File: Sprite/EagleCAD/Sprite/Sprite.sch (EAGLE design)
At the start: 32 parts, among them P1 SPRITE_PIN, P2 SPRITE_PIN, U1 CC430F5137, U2 HMC5883LSMD, U3 ITG-3200

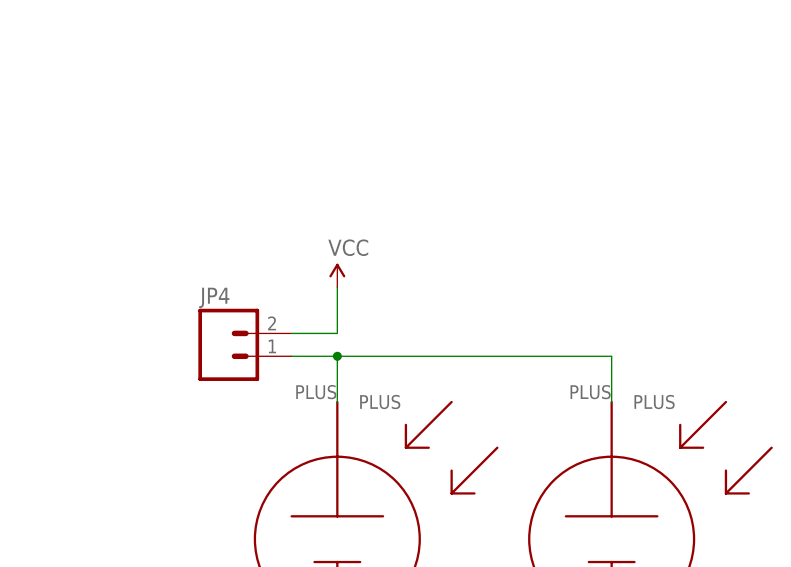
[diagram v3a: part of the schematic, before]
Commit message: Made corner hole 2.8 mm
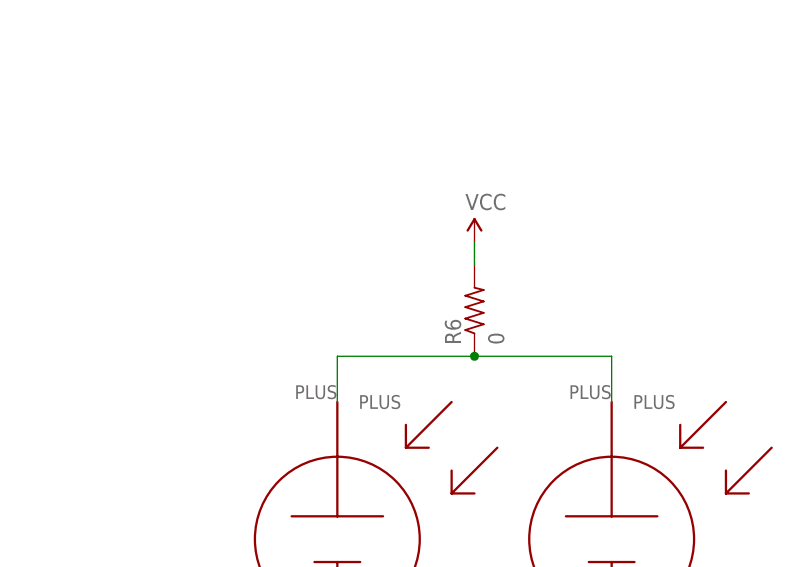
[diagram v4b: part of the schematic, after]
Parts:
- removed JP4: (no value), SparkFun:M02PTH
- added R6: 0, rcl:R-US_R0805
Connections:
- net VCC: now also R6.2; no longer JP4.2
- net VSOLAR: now also R6.1; no longer JP4.1
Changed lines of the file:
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@@
 <part name="GND10" library="SparkFun" deviceset="GND" device=""/>
 <part name="R5" library="SparkFun" deviceset="RESISTOR" device="0603-RES" value="270R"/>
-<part name="JP4" library="SparkFun" deviceset="M02" device="PTH"/>
 <part name="JP3" library="SparkFun" deviceset="M02" device="PTH"/>
-<part name="S2" library="TASC" deviceset="TASC" device=""/>
 <part name="U$1" library="SpriteTCXO" deviceset="TCXO_7Z" device=""/>
 <part name="P+11" library="SparkFun" deviceset="VCC" device=""/>
@@
 <part name="P1" library="SpritePin" deviceset="SPRITE_PIN" device=""/>
 <part name="S1" library="TASC" deviceset="TASC" device=""/>
+<part name="S2" library="TASC" deviceset="TASC" device=""/>
+<part name="R6" library="rcl" deviceset="R-US_" device="R0805" value="0"/>
 </parts>
 <sheets>
@@
 <instances>
 <instance part="GND1" gate="1" x="347.98" y="66.04"/>
-<instance part="P+1" gate="1" x="332.74" y="114.3"/>
+<instance part="P+1" gate="1" x="347.98" y="119.38"/>
 <instance part="U1" gate="G$1" x="152.4" y="86.36"/>
 <instance part="C1" gate="G$1" x="228.6" y="55.88" rot="R90"/>
@@
 <instance part="GND10" gate="1" x="86.36" y="99.06"/>
 <instance part="R5" gate="G$1" x="104.14" y="104.14"/>
-<instance part="JP4" gate="G$1" x="320.04" y="106.68"/>
 <instance part="JP3" gate="G$1" x="114.3" y="88.9" rot="MR180"/>
-<instance part="S2" gate="G$1" x="332.74" y="86.36"/>
 <instance part="U$1" gate="G$1" x="241.3" y="50.8" rot="MR0"/>
 <instance part="P+11" gate="1" x="251.46" y="48.26"/>
 <instance part="P2" gate="G$1" x="127" y="144.78"/>
 <instance part="P1" gate="G$1" x="127" y="137.16"/>
-<instance part="S1" gate="G$1" x="363.22" y="86.36"/>
+<instance part="S1" gate="G$1" x="332.74" y="86.36"/>
+<instance part="S2" gate="G$1" x="363.22" y="86.36"/>
+<instance part="R6" gate="G$1" x="347.98" y="111.76" rot="R90"/>
 </instances>
 <busses>
@@
 </segment>
 <segment>
-<pinref part="JP4" gate="G$1" pin="2"/>
 <pinref part="P+1" gate="1" pin="VCC"/>
-<wire x1="327.66" y1="109.22" x2="332.74" y2="109.22" width="0.1524" layer="91"/>
-<wire x1="332.74" y1="109.22" x2="332.74" y2="114.3" width="0.1524" layer="91"/>
+<pinref part="R6" gate="G$1" pin="2"/>
+<wire x1="347.98" y1="116.84" x2="347.98" y2="119.38" width="0.1524" layer="91"/>
 </segment>
 <segment>
@@
 </segment>
 <segment>
-<pinref part="S2" gate="G$1" pin="MINUS1"/>
 <wire x1="327.66" y1="71.12" x2="327.66" y2="68.58" width="0.1524" layer="91"/>
-<pinref part="S2" gate="G$1" pin="MINUS2"/>
 <wire x1="327.66" y1="68.58" x2="347.98" y2="68.58" width="0.1524" layer="91"/>
 <wire x1="347.98" y1="68.58" x2="337.82" y2="68.58" width="0.1524" layer="91"/>
@@
 <junction x="347.98" y="68.58"/>
 <junction x="337.82" y="68.58"/>
-<pinref part="S1" gate="G$1" pin="MINUS2"/>
 <wire x1="368.3" y1="71.12" x2="368.3" y2="68.58" width="0.1524" layer="91"/>
-<pinref part="S1" gate="G$1" pin="MINUS1"/>
 <wire x1="358.14" y1="71.12" x2="358.14" y2="68.58" width="0.1524" layer="91"/>
 <wire x1="368.3" y1="68.58" x2="358.14" y2="68.58" width="0.1524" layer="91"/>
@@
 <junction x="358.14" y="68.58"/>
 <junction x="368.3" y="68.58"/>
+<pinref part="S1" gate="G$1" pin="MINUS1"/>
+<pinref part="S1" gate="G$1" pin="MINUS2"/>
+<pinref part="S2" gate="G$1" pin="MINUS1"/>
+<pinref part="S2" gate="G$1" pin="MINUS2"/>
 </segment>
 <segment>
@@
 <net name="VSOLAR" class="0">
 <segment>
-<pinref part="JP4" gate="G$1" pin="1"/>
-<wire x1="327.66" y1="106.68" x2="332.74" y2="106.68" width="0.1524" layer="91"/>
+<wire x1="332.74" y1="101.6" x2="332.74" y2="106.68" width="0.1524" layer="91"/>
+<wire x1="363.22" y1="101.6" x2="363.22" y2="106.68" width="0.1524" layer="91"/>
+<wire x1="363.22" y1="106.68" x2="347.98" y2="106.68" width="0.1524" layer="91"/>
+<pinref part="S1" gate="G$1" pin="PLUS"/>
 <pinref part="S2" gate="G$1" pin="PLUS"/>
-<wire x1="332.74" y1="101.6" x2="332.74" y2="106.68" width="0.1524" layer="91"/>
-<pinref part="S1" gate="G$1" pin="PLUS"/>
-<wire x1="363.22" y1="101.6" x2="363.22" y2="106.68" width="0.1524" layer="91"/>
-<wire x1="363.22" y1="106.68" x2="332.74" y2="106.68" width="0.1524" layer="91"/>
-<junction x="332.74" y="106.68"/>
-</segment>
-</net>
+<pinref part="R6" gate="G$1" pin="1"/>
+<wire x1="347.98" y1="106.68" x2="332.74" y2="106.68" width="0.1524" layer="91"/>
+<junction x="347.98" y="106.68"/>
+</segment>
+</net>

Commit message: Updated Gerbers and BOM for new Sprite order
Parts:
- renumbered U$1 to X1
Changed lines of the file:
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@@
 <part name="R5" library="SparkFun" deviceset="RESISTOR" device="0603-RES" value="270R"/>
 <part name="JP3" library="SparkFun" deviceset="M02" device="PTH"/>
-<part name="U$1" library="SpriteTCXO" deviceset="TCXO_7Z" device=""/>
+<part name="X1" library="SpriteTCXO" deviceset="TCXO_7Z" device=""/>
 <part name="P+11" library="SparkFun" deviceset="VCC" device=""/>
 <part name="P2" library="SpritePin" deviceset="SPRITE_PIN" device=""/>
@@
 <instance part="R5" gate="G$1" x="104.14" y="104.14"/>
 <instance part="JP3" gate="G$1" x="114.3" y="88.9" rot="MR180"/>
-<instance part="U$1" gate="G$1" x="241.3" y="50.8" rot="MR0"/>
+<instance part="X1" gate="G$1" x="241.3" y="50.8" rot="MR0"/>
 <instance part="P+11" gate="1" x="251.46" y="48.26"/>
 <instance part="P2" gate="G$1" x="127" y="144.78"/>
@@
 </segment>
 <segment>
-<pinref part="U$1" gate="G$1" pin="VCC"/>
+<pinref part="X1" gate="G$1" pin="VCC"/>
 <pinref part="P+11" gate="1" pin="VCC"/>
 <wire x1="248.92" y1="45.72" x2="251.46" y2="45.72" width="0.1524" layer="91"/>
@@
 </segment>
 <segment>
-<pinref part="U$1" gate="G$1" pin="GND"/>
+<pinref part="X1" gate="G$1" pin="GND"/>
 <pinref part="GND8" gate="1" pin="GND"/>
 <wire x1="226.06" y1="45.72" x2="233.68" y2="45.72" width="0.1524" layer="91"/>
@@
 <segment>
 <pinref part="C1" gate="G$1" pin="2"/>
-<pinref part="U$1" gate="G$1" pin="OUT"/>
+<pinref part="X1" gate="G$1" pin="OUT"/>
 <wire x1="231.14" y1="55.88" x2="233.68" y2="55.88" width="0.1524" layer="91"/>
 </segment>

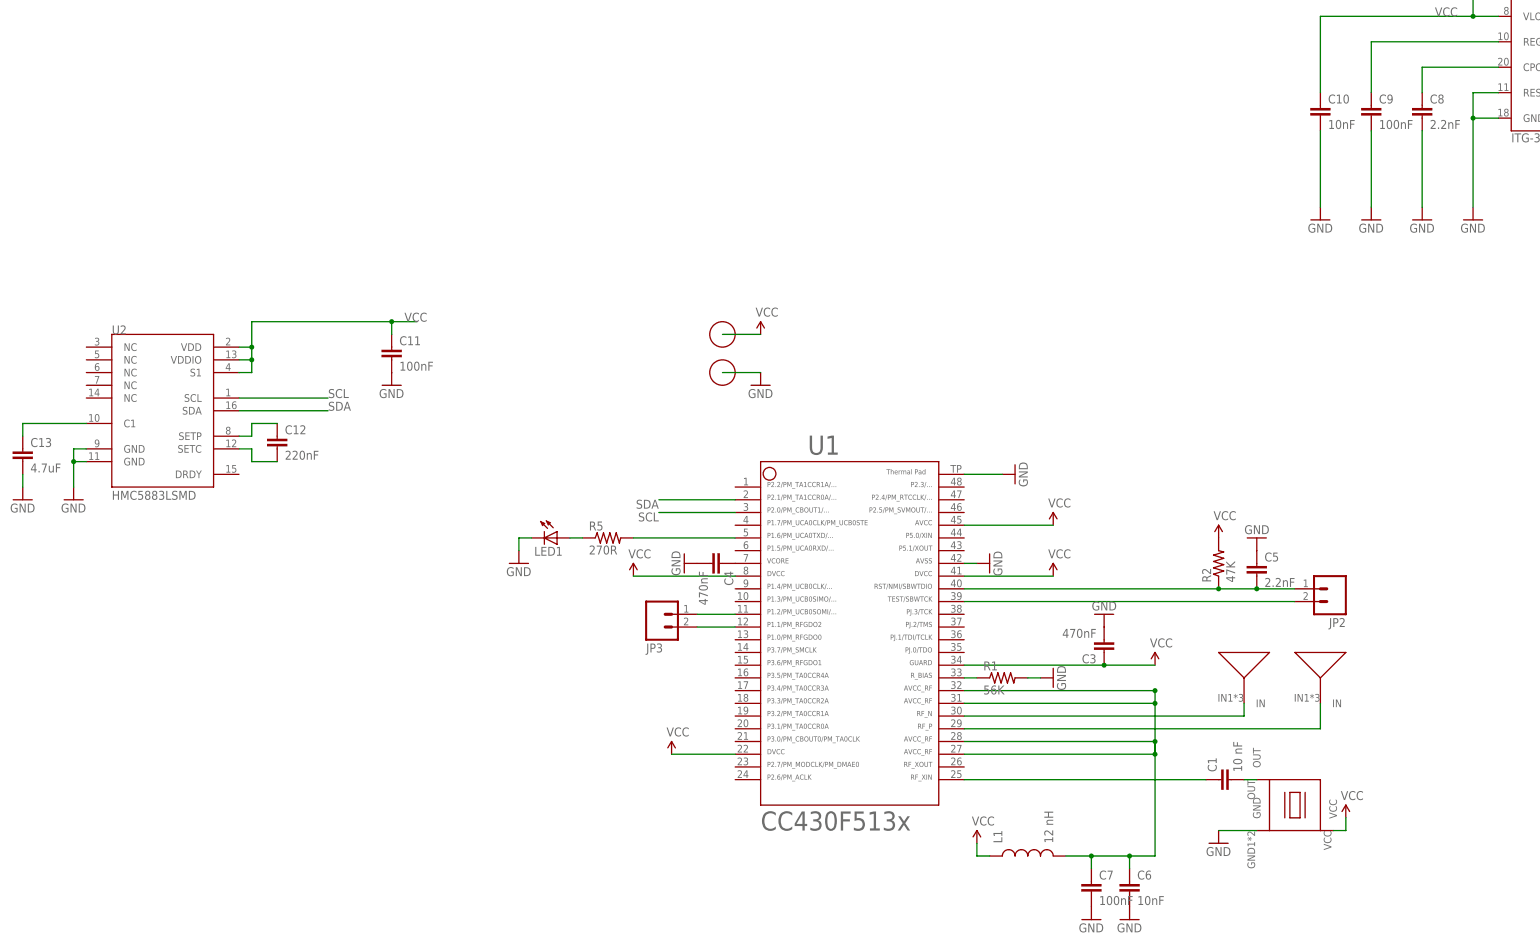
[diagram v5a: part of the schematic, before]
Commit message: Fixed silksreen on Sprite board
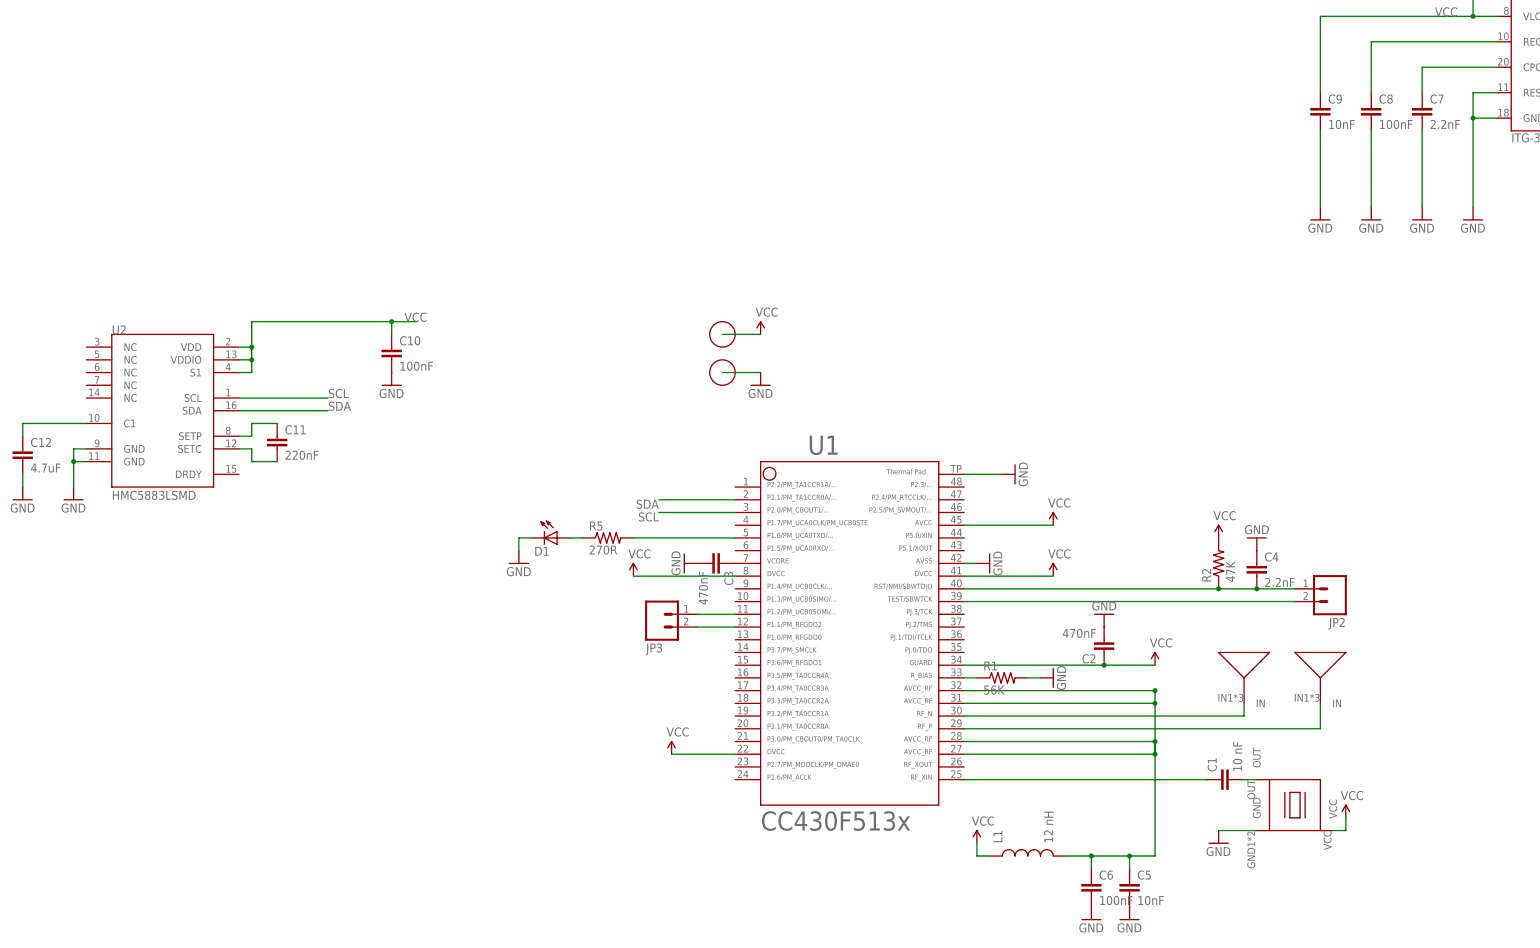
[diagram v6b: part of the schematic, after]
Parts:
- removed C13: 4.7uF, SparkFun:CAP0603-CAP
- added C2: 470nF, SparkFun:CAP0603-CAP
- C10, C6: value 10nF -> 100nF
- C11: value 100nF -> 220nF
- C12: value 220nF -> 4.7uF
- C4: value 470nF -> 2.2nF
- C5: value 2.2nF -> 10nF
- C7: value 100nF -> 2.2nF
- C8: value 2.2nF -> 100nF
- C9: value 100nF -> 10nF
- renumbered LED1 to D1
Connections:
- net GND: now also C12.2, C2.2, C4.1, C5.2; no longer C11.2, C13.2, C4.2, C5.1
- net N$4: now also C3.1; no longer C4.1
- net N$5: now also C11.1; no longer C12.1
- net N$6: now also C11.2; no longer C12.2
- net N$7: now also C12.1; no longer C13.1
- net N$8: now also C7.1; no longer C8.1
- net N$9: now also C8.1; no longer C9.1
- net RST: now also C4.2; no longer C5.2
- net VCC: now also C2.1, C9.1; no longer C11.1, C3.1
- net VCCRF: now also C5.1; no longer C7.1
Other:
- moved on the sheet: C10, C11, C12, C3, C4, C5, C6, C7, C8, C9
